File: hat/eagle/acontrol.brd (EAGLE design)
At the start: 65.3 x 30.7 mm, 8 parts, among them J1 RASPBERRYPI-40-PIN-GPIO_PTH_N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, J4 4P-2.0-90D, J5 GREEN-2P-3.5, J7 455-1750-1-ND, U1 TXB0104

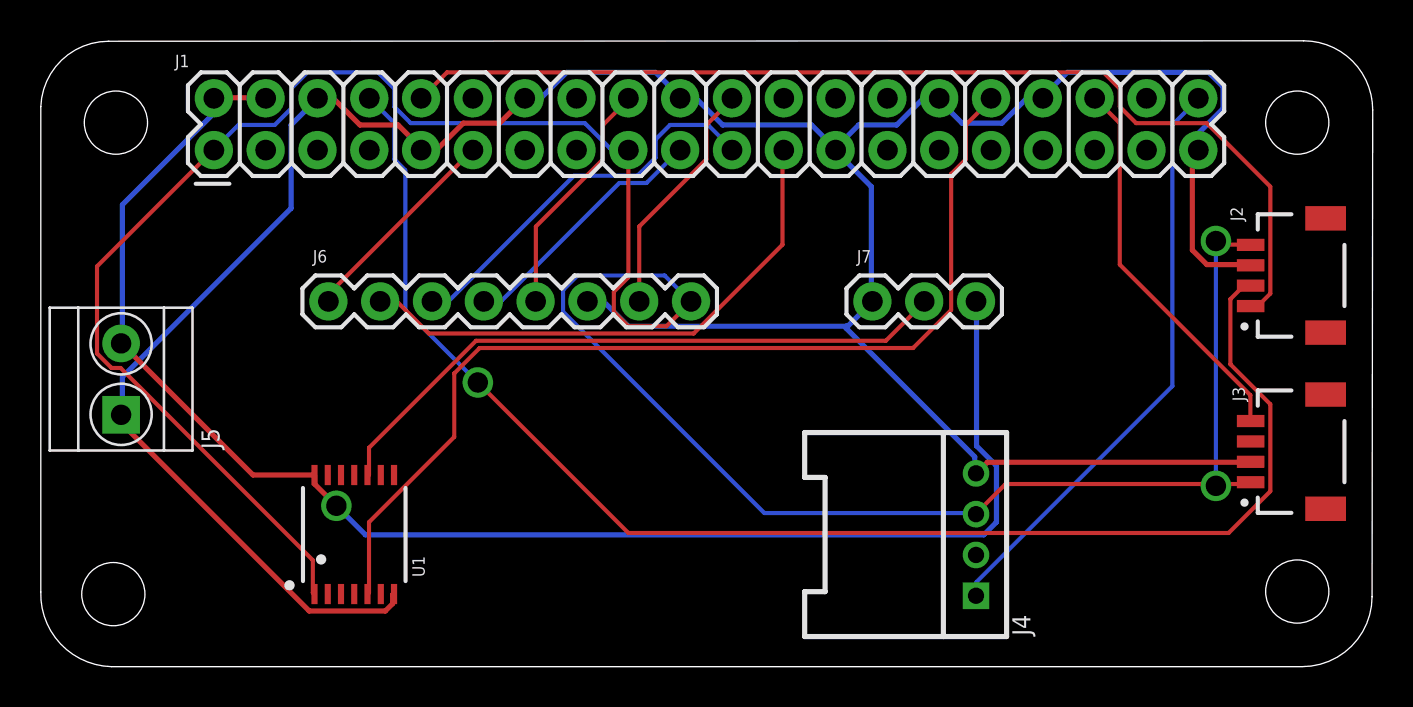
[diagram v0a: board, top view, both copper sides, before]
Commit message: uHat corrections + 3D printed case
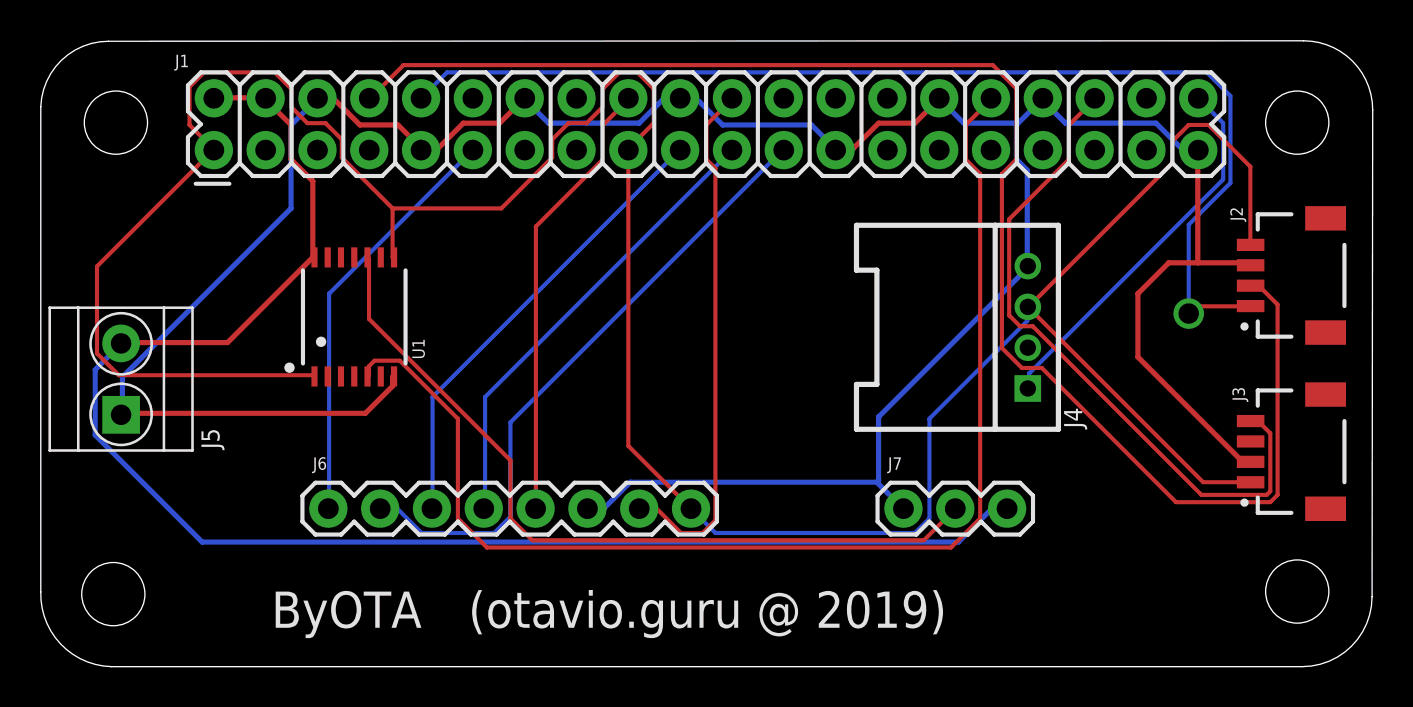
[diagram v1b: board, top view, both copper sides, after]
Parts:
- moved U1 10.7 mm to (66.0, 51.3)
- moved J4 10.5 mm to (99.1, 50.8)
- moved J7 10.3 mm to (93.0, 41.9)
- moved J6 10.2 mm to (64.8, 41.9)
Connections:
- net 3.3V: now also U1.8
- net MFRC522_MISO: now also J1.21; no longer J1.19
- net MFRC522_MOSI: now also J1.19; no longer J1.21
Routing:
- net 3.3V: track 126.8 -> 142.1 mm, vias 2 -> 0
- net MFRC522_RESET: track 11.8 -> 25.9 mm
- net GT_IPCCK: track 19.0 -> 33.0 mm
- net BUZZER_IN: track 28.9 -> 18.7 mm
- net MFRC522_IRQ: track 11.8 -> 22.0 mm
- net MFRC522_SDA: track 10.4 -> 20.5 mm
- net MFRC522_MISO: track 12.7 -> 22.6 mm
- net NEOPIXEL_IN: track 49.4 -> 59.3 mm
- net NEOPIXEL_OUT: track 31.6 -> 38.6 mm
- net GT_TX: track 51.5 -> 55.4 mm, vias 0 -> 1
- net MFRC522_SCK: track 26.9 -> 30.8 mm
- net GND: track 148.0 -> 144.6 mm
- net GT_RX: track 70.4 -> 73.7 mm, vias 1 -> 0
- net MFRC522_MOSI: track 19.4 -> 22.6 mm
- net 5V: track 75.0 -> 75.1 mm, vias 1 -> 0
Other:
- board text added: "(otavio.guru @ 2019)"
- board text added: "ByOTA"
